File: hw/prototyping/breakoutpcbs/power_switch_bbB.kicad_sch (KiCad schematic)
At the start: 17 parts, among them J3 Conn_01x07, J4 Conn_01x02, Q1 BC337, Q2 BC847, U2 BD48ExxG, U3 L7805, U4 XC6220B331MR, U5 MAX40200AUK

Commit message: refactoring of the current boards and two added to test the whole circuit
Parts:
- added C4, C5, C6: 22uF, Capacitor_SMD:C_0805_2012Metric_Pad1.18x1.45mm_HandSolder, symbol Device:C
- added R31, R32, R57: 10k, Resistor_SMD:R_0805_2012Metric_Pad1.20x1.40mm_HandSolder, symbol Device:R
- added R46, R48: 0R, Resistor_SMD:R_0805_2012Metric_Pad1.20x1.40mm_HandSolder, symbol Device:R
- added R47: 4k2, Resistor_SMD:R_0805_2012Metric_Pad1.20x1.40mm_HandSolder, symbol Device:R
- added U7: BD48ExxG, Package_TO_SOT_SMD:SOT-23-5, symbol Power_Management:BD48ExxG
- R5: value 47k -> 10k
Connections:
- net +3V3_1: now also C4.1, C5.1, C6.1
- net EN: now also J3.5 (Pin_5), R32.1, U7.1 (VOUT); no longer J3.6 (Pin_6), R5.1, R6.1, R7.1, U2.1 (VOUT)
- net GND2: now also J3.6 (Pin_6), C4.2, C5.2, C6.2, R57.2, U7.3 (GND); no longer J3.7 (Pin_7)
- net RUNNING: now also R46.2, R48.2; no longer Q1.1 (C), Q2.3 (C)
- net VBUS: now also J3.7 (Pin_7), R31.1; no longer J3.5 (Pin_5), U2.2 (VDD)
- net at Q1.2 (B), Q2.1 (B), R6.2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: now also R46.1
- new net: R31.2, R32.2, R57.1, U2.2 (VDD), U7.2 (VDD)
- new net: Q1.1 (C), Q2.3 (C), R47.1, R48.1
- new net: R47.2, R5.1, R6.1, R7.1, U2.1 (VOUT)
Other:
- note added: "adjust the threshold to 4V"
- moved on the sheet: Q1, Q2, R10, R5, R6, R7, R9, U2

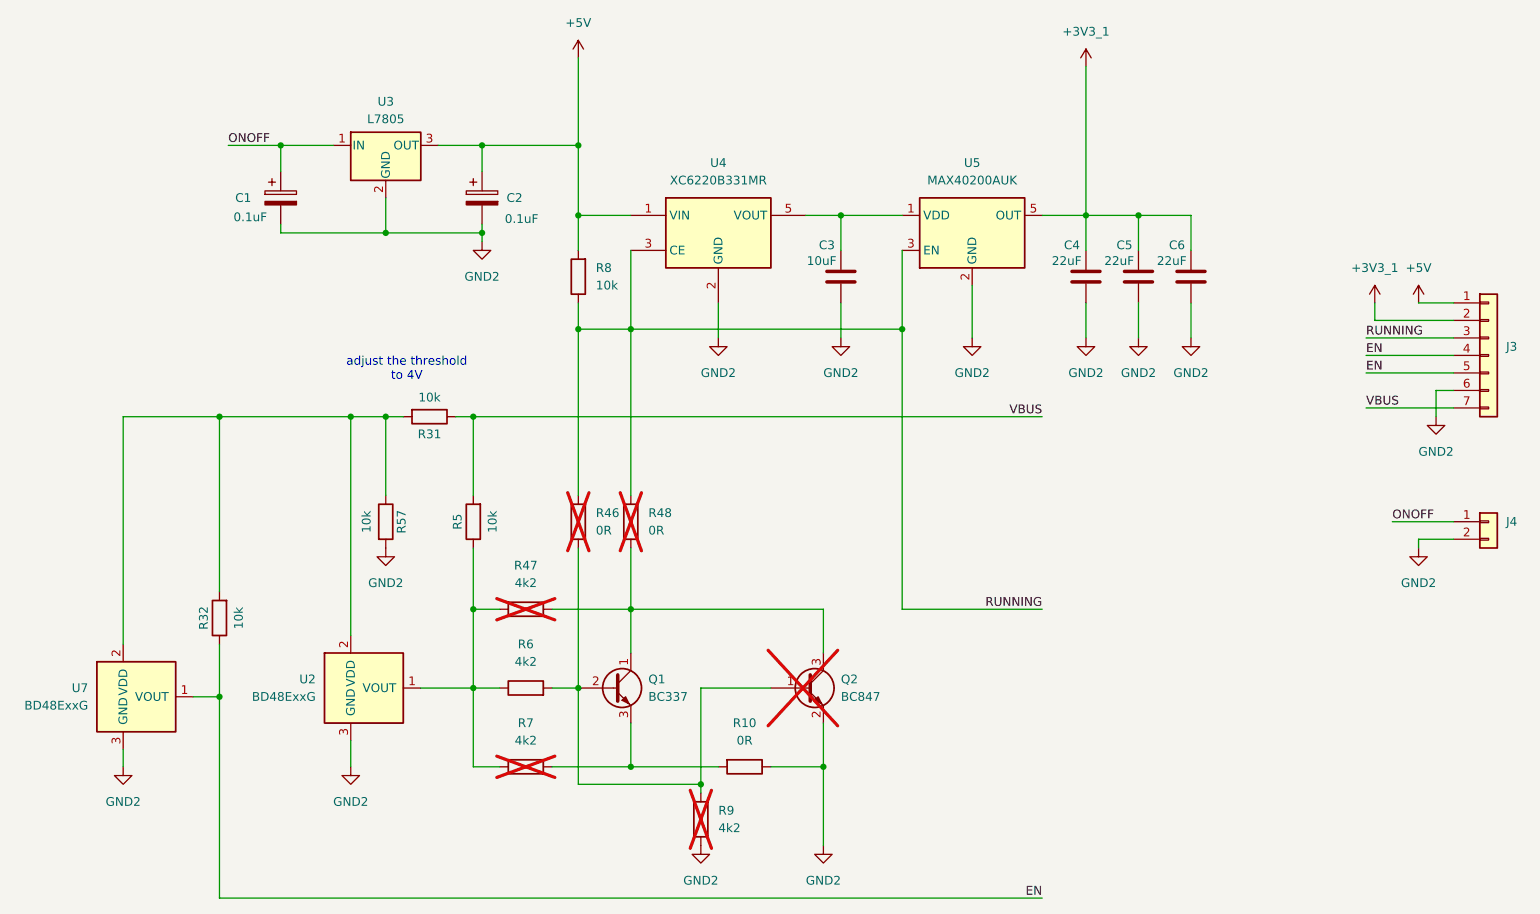
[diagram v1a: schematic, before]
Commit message: updated schematics
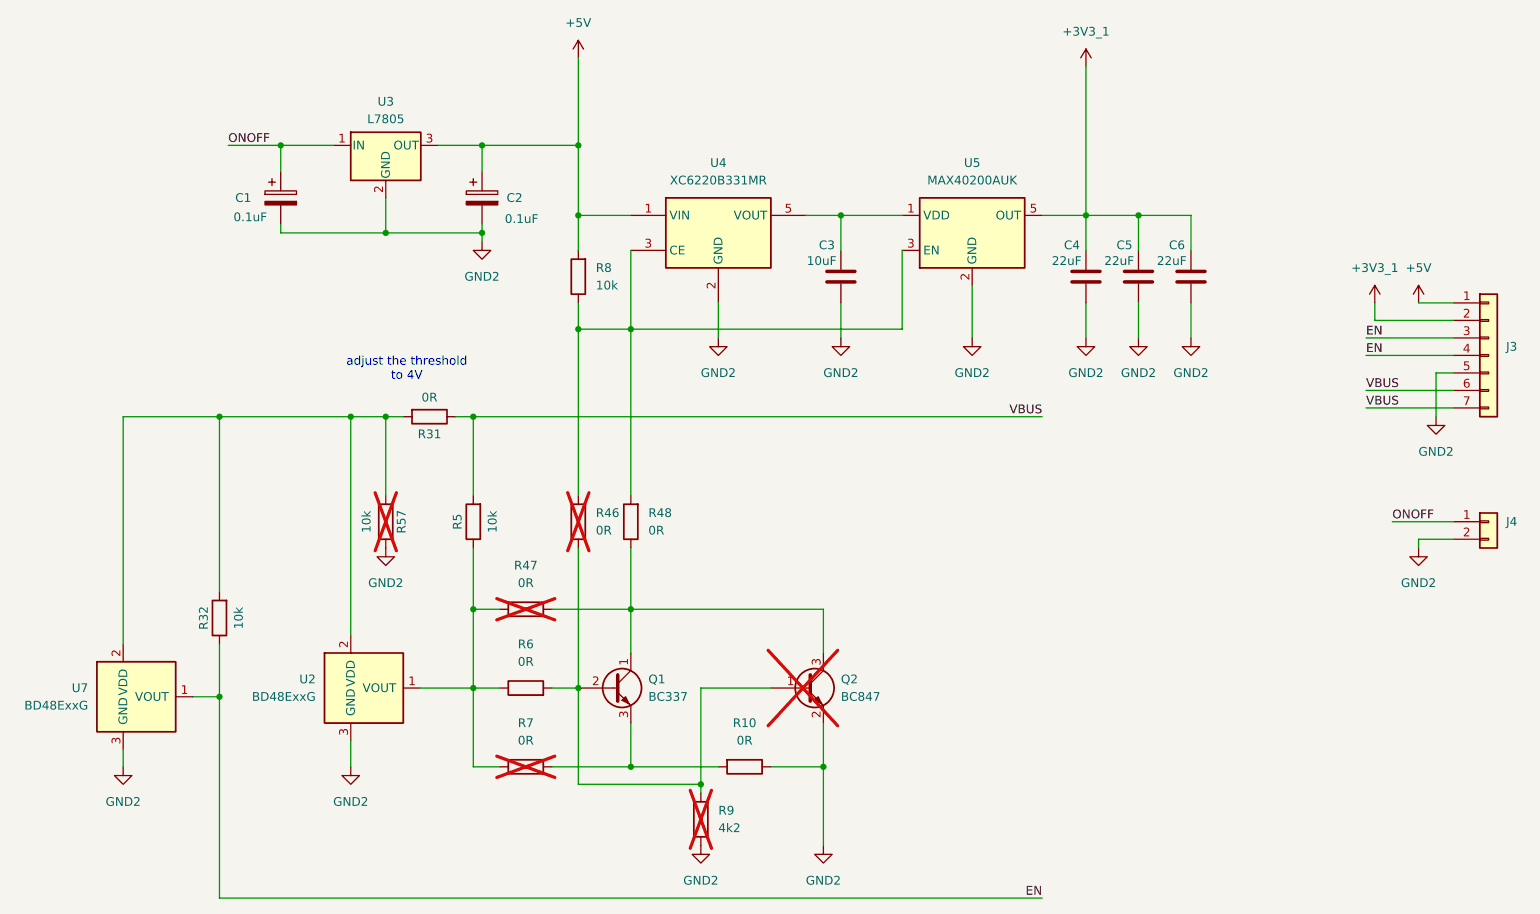
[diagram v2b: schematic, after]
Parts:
- R31: value 10k -> 0R
- R47, R6, R7: value 4k2 -> 0R
- R48: now fitted
- R57: now not fitted
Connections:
- net EN: now also J3.3 (Pin_3); no longer J3.5 (Pin_5)
- net GND2: now also J3.5 (Pin_5); no longer J3.6 (Pin_6)
- net VBUS: now also J3.6 (Pin_6)
- net RUNNING: no longer names the net of R46.2, R48.2, R8.1, U4.3 (CE), U5.3 (EN)
- net RUNNING: no longer J3.3 (Pin_3)
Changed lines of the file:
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@@
 	)
 	(junction
-		(at 147.32 74.93)
-		(diameter 0)
-		(color 0 0 0 0)
-	)
-	(junction
 		(at 86.36 60.96)
 		(diameter 0)
@@
 	(wire
 		(pts
-			(xy 147.32 115.57) (xy 147.32 74.93)
-		)
-		(stroke
-			(width 0)
-			(type default)
-		)
-	)
-	(wire
-		(pts
 			(xy 57.15 48.26) (xy 64.77 48.26)
 		)
@@
 	(wire
 		(pts
-			(xy 214.63 78.74) (xy 227.33 78.74)
+			(xy 214.63 76.2) (xy 227.33 76.2)
 		)
 		(stroke
@@
 	(wire
 		(pts
+			(xy 214.63 86.36) (xy 227.33 86.36)
+		)
+		(stroke
+			(width 0)
+			(type default)
+		)
+	)
+	(wire
+		(pts
 			(xy 44.45 128.27) (xy 48.26 128.27)
 		)
@@
 	(wire
 		(pts
-			(xy 107.95 138.43) (xy 120.65 138.43)
+			(xy 224.79 81.28) (xy 227.33 81.28)
 		)
 		(stroke
@@
 	(wire
 		(pts
-			(xy 224.79 83.82) (xy 224.79 87.63)
+			(xy 107.95 138.43) (xy 120.65 138.43)
 		)
 		(stroke
@@
 	(wire
 		(pts
-			(xy 214.63 86.36) (xy 227.33 86.36)
+			(xy 214.63 83.82) (xy 227.33 83.82)
 		)
 		(stroke
@@
 	(wire
 		(pts
-			(xy 214.63 81.28) (xy 227.33 81.28)
+			(xy 214.63 78.74) (xy 227.33 78.74)
 		)
 		(stroke
@@
 	(wire
 		(pts
-			(xy 167.64 115.57) (xy 147.32 115.57)
-		)
-		(stroke
-			(width 0)
-			(type default)
-		)
-	)
-	(wire
-		(pts
 			(xy 57.15 60.96) (xy 57.15 59.69)
 		)
@@
 	(wire
 		(pts
-			(xy 227.33 83.82) (xy 224.79 83.82)
-		)
-		(stroke
-			(width 0)
-			(type default)
-		)
-	)
-	(wire
-		(pts
 			(xy 77.47 127) (xy 85.09 127)
 		)
@@
 	(wire
 		(pts
-			(xy 214.63 76.2) (xy 227.33 76.2)
+			(xy 48.26 157.48) (xy 48.26 128.27)
 		)
 		(stroke
@@
 	(wire
 		(pts
-			(xy 48.26 157.48) (xy 48.26 128.27)
+			(xy 224.79 81.28) (xy 224.79 87.63)
 		)
 		(stroke
@@
 		)
 	)
-	(label "RUNNING"
-		(at 214.63 76.2 0)
+	(label "EN"
+		(at 167.64 157.48 180)
 		(effects
 			(font
 				(size 1.27 1.27)
 			)
-			(justify left bottom)
+			(justify right bottom)
 		)
 	)
-	(label "RUNNING"
-		(at 167.64 115.57 180)
+	(label "VBUS"
+		(at 214.63 83.82 0)
 		(effects
 			(font
 				(size 1.27 1.27)
 			)
-			(justify right bottom)
+			(justify left bottom)
 		)
 	)
-	(label "EN"
-		(at 167.64 157.48 180)
+	(label "VBUS"
+		(at 167.64 87.63 180)
 		(effects
 			(font
@@
 		)
 	)
-	(label "VBUS"
-		(at 167.64 87.63 180)
-		(effects
-			(font
-				(size 1.27 1.27)
-			)
-			(justify right bottom)
-		)
-	)
 	(label "ONOFF"
 		(at 49.53 48.26 0)
@@
 	)
 	(label "EN"
-		(at 214.63 81.28 0)
+		(at 214.63 78.74 0)
 		(effects
 			(font
@@
 	)
 	(label "EN"
-		(at 214.63 78.74 0)
+		(at 214.63 76.2 0)
 		(effects
 			(font
@@
 			)
 		)
-		(property "Value" "10k"
+		(property "Value" "0R"
 			(at 78.74 84.836 90)
 			(effects
@@
 			)
 		)
-		(property "Value" "4k2"
+		(property "Value" "0R"
 			(at 92.71 111.76 90)
 			(effects
@@
 		(in_bom yes)
 		(on_board yes)
-		(dnp no)
+		(dnp yes)
 		(property "Reference" "R57"
 			(at 74.676 102.87 90)
@@
 		(in_bom yes)
 		(on_board yes)
-		(dnp yes)
+		(dnp no)
 		(fields_autoplaced yes)
 		(property "Reference" "R48"
@@
 			)
 		)
-		(property "Value" "4k2"
+		(property "Value" "0R"
 			(at 92.71 123.19 90)
 			(effects
@@
 			)
 		)
-		(property "Value" "4k2"
+		(property "Value" "0R"
 			(at 92.71 134.62 90)
 			(effects
